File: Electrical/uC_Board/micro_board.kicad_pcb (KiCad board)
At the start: 2 copper layers, 45 x 18 mm, 26 parts, among them J1 card_edge_6p, Q1 BC850, SW1 SW_Push, U1 ATmega328PB-AU, U2 ArdStripNano, U3 CSTNE16M0V530000R0, U4 AD8620, U5 LM1117MPX-5.0

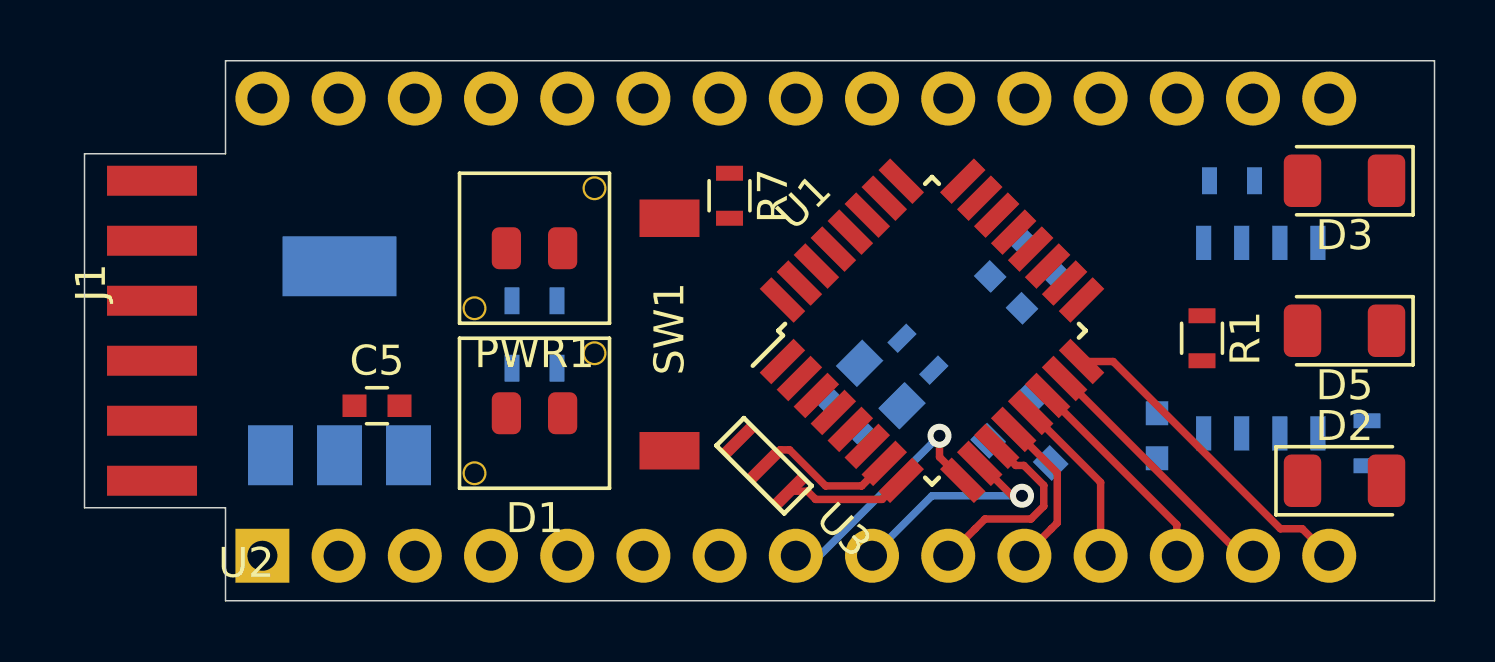
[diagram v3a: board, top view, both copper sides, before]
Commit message: adding traces, removed auto selector, changed diode footprints
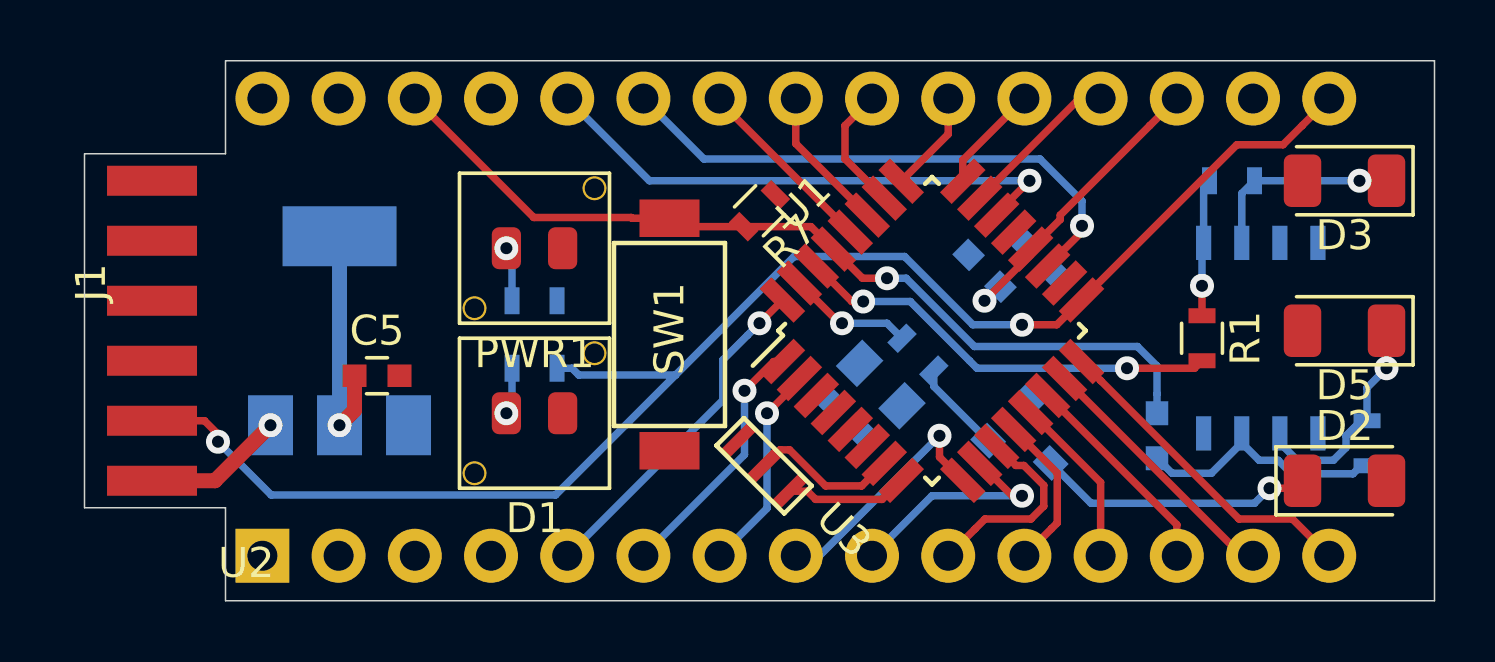
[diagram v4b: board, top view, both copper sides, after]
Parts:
- moved R7 1.12 mm to (122.5, 96.0), turned to 225 degrees
- moved C4 1.02 mm to (130.0, 98.0), turned to 135 degrees
- moved C5 1.00 mm to (109.8, 101.5)
- moved U5 1.00 mm to (108.5, 100.0)
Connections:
- C4 pad 1: Net-(C4-Pad1) -> /AREF
- U1 pad 20: Net-(C4-Pad1) -> /AREF
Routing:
- net /D13: track 0.00 -> 51.8 mm, vias 0 -> 2
- net /RESET: track 0.00 -> 30.0 mm, vias 0 -> 1
- net /A6: track 0.00 -> 18.7 mm, vias 0 -> 1
- net /A7: track 0.00 -> 18.1 mm, vias 0 -> 1
- net /D0: track 0.00 -> 14.4 mm, vias 0 -> 2
- net /D2: track 0.00 -> 11.5 mm, vias 0 -> 1
- net /AREF: track 0.00 -> 10.1 mm, vias 0 -> 1
- net Net-(D2-Pad1): track 0.00 -> 9.26 mm, vias 0 -> 1
- net /D3: track 0.00 -> 8.56 mm, vias 0 -> 1
- net Net-(C6-Pad1): track 0.00 -> 8.48 mm
- net +5V: track 0.00 -> 8.16 mm, vias 0 -> 1
- net Net-(D5-Pad1): track 0.00 -> 7.51 mm, vias 0 -> 1
- net /D4: track 0.00 -> 7.01 mm, vias 0 -> 1
- net Net-(D3-Pad1): track 0.00 -> 6.65 mm, vias 0 -> 1
- net /A5: track 0.00 -> 6.26 mm
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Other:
- net class power added: clearance 0.2, trace_width 0.5, via_dia 0.8, via_drill 0.4

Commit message: i have no idea where these last traces are supposed to go
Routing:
- net /RESET: track 30.0 -> 43.7 mm
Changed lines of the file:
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@@
     (thickness 1.6)
     (drawings 9)
-    (tracks 198)
+    (tracks 202)
     (zones 0)
     (modules 26)
@@
     (38 B.Mask user)
     (39 F.Mask user)
-    (40 Dwgs.User user)
+    (40 Dwgs.User user hide)
     (41 Cmts.User user)
     (42 Eco1.User user)
@@
   (segment (start 114.97499 96.22499) (end 118.22499 96.22499) (width 0.25) (layer F.Cu) (net 5))
   (segment (start 111.01 92.26) (end 114.97499 96.22499) (width 0.25) (layer F.Cu) (net 5))
+  (segment (start 113.58316 96.22499) (end 114.97499 96.22499) (width 0.25) (layer F.Cu) (net 5))
+  (segment (start 111.909999 97.898151) (end 113.58316 96.22499) (width 0.25) (layer F.Cu) (net 5))
+  (segment (start 111.909999 106.600001) (end 111.909999 97.898151) (width 0.25) (layer F.Cu) (net 5))
+  (segment (start 111.01 107.5) (end 111.909999 106.600001) (width 0.25) (layer F.Cu) (net 5))
   (segment (start 138.578427 107.5) (end 138.95 107.5) (width 0.25) (layer F.Cu) (net 6))
   (segment (start 132.669417 101.59099) (end 138.578427 107.5) (width 0.25) (layer F.Cu) (net 6))

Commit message: forgot a file
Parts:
- moved C5 1.25 mm to (109.8, 100.2)
- moved U5 1.25 mm to (108.5, 98.8)
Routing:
- net /D1: track 4.18 -> 30.0 mm
- net VCC: track 4.72 -> 0.00 mm, vias 1 -> 0
- net /RESET: track 43.7 -> 44.1 mm, vias 1 -> 2
- net /D13: track 51.8 -> 51.7 mm, vias 2 -> 4
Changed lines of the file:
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@@
     (thickness 1.6)
     (drawings 9)
-    (tracks 202)
+    (tracks 219)
     (zones 0)
     (modules 26)
@@
   )
   (module hodgkin:LM1117 (layer B.Cu)
-    (at 108.5 100 90)
+    (at 108.5 98.75 90)
     (descr "module CMS SOT223 4 pins")
     (tags "CMS SOT")
@@
   )
   (module Capacitors_SMD:C_0603 (layer F.Cu)
-    (at 109.75 101.5)
+    (at 109.75 100.25)
     (descr "Capacitor SMD 0603, reflow soldering, AVX (see smccp.pdf)")
     (tags "capacitor 0603")
@@
   (gr_line (start 145 91) (end 145 109) (layer Edge.Cuts) (width 0.05))
   (gr_line (start 104.7 109) (end 145 109) (layer Edge.Cuts) (width 0.05))
-  (via (at 106.2 103.15) (size 0.8) (drill 0.4) (layers F.Cu B.Cu) (net 2))
-  (segment (start 104.35 105) (end 102.25 105) (width 0.5) (layer F.Cu) (net 2))
-  (segment (start 106.2 103.15) (end 104.35 105) (width 0.5) (layer F.Cu) (net 2))
   (via (at 114.0625 102.75) (size 0.8) (drill 0.4) (layers F.Cu B.Cu) (net 3))
   (segment (start 114.25 101.25) (end 114.25 102.5625) (width 0.25) (layer B.Cu) (net 3))
@@
   (segment (start 111.01 92.26) (end 114.97499 96.22499) (width 0.25) (layer F.Cu) (net 5))
   (segment (start 113.58316 96.22499) (end 114.97499 96.22499) (width 0.25) (layer F.Cu) (net 5))
-  (segment (start 111.909999 97.898151) (end 113.58316 96.22499) (width 0.25) (layer F.Cu) (net 5))
-  (segment (start 111.909999 106.600001) (end 111.909999 97.898151) (width 0.25) (layer F.Cu) (net 5))
-  (segment (start 111.01 107.5) (end 111.909999 106.600001) (width 0.25) (layer F.Cu) (net 5))
+  (via (at 113 96.25) (size 0.8) (drill 0.4) (layers F.Cu B.Cu) (net 5))
+  (segment (start 111.909999 97.340001) (end 113 96.25) (width 0.25) (layer B.Cu) (net 5))
+  (segment (start 111.01 107.5) (end 111.909999 106.600001) (width 0.25) (layer B.Cu) (net 5))
+  (segment (start 111.909999 106.600001) (end 111.909999 97.340001) (width 0.25) (layer B.Cu) (net 5))
+  (segment (start 113.58316 96.232525) (end 113.58316 96.22499) (width 0.25) (layer F.Cu) (net 5))
+  (segment (start 113.565685 96.25) (end 113.58316 96.232525) (width 0.25) (layer F.Cu) (net 5))
+  (segment (start 113 96.25) (end 113.565685 96.25) (width 0.25) (layer F.Cu) (net 5))
   (segment (start 138.578427 107.5) (end 138.95 107.5) (width 0.25) (layer F.Cu) (net 6))
   (segment (start 132.669417 101.59099) (end 138.578427 107.5) (width 0.25) (layer F.Cu) (net 6))
@@
   (segment (start 132.409799 99.799999) (end 133.235103 98.974695) (width 0.25) (layer F.Cu) (net 7))
   (segment (start 131.25 99.799999) (end 132.409799 99.799999) (width 0.25) (layer F.Cu) (net 7))
-  (via (at 104.448959 103.698959) (size 0.8) (drill 0.4) (layers F.Cu B.Cu) (net 7))
-  (segment (start 104.448959 103.448959) (end 104.448959 103.698959) (width 0.25) (layer F.Cu) (net 7))
-  (segment (start 102.25 103) (end 104 103) (width 0.25) (layer F.Cu) (net 7))
-  (segment (start 104 103) (end 104.448959 103.448959) (width 0.25) (layer F.Cu) (net 7))
-  (segment (start 115.701997 105.475001) (end 119.701997 101.475001) (width 0.25) (layer B.Cu) (net 7))
-  (segment (start 106.225001 105.475001) (end 115.701997 105.475001) (width 0.25) (layer B.Cu) (net 7))
-  (segment (start 104.448959 103.698959) (end 106.225001 105.475001) (width 0.25) (layer B.Cu) (net 7))
-  (segment (start 108.5 96.85) (end 108.5 103.15) (width 0.5) (layer B.Cu) (net 8))
-  (via (at 108.5 103.15) (size 0.8) (drill 0.4) (layers F.Cu B.Cu) (net 8))
-  (segment (start 109 101.5) (end 109 102.65) (width 0.5) (layer F.Cu) (net 8))
-  (segment (start 109 102.65) (end 108.5 103.15) (width 0.5) (layer F.Cu) (net 8))
+  (via (at 118.75 102.25) (size 0.8) (drill 0.4) (layers F.Cu B.Cu) (net 7))
+  (segment (start 119.701997 101.475001) (end 119.524999 101.475001) (width 0.25) (layer B.Cu) (net 7))
+  (segment (start 119.524999 101.475001) (end 118.75 102.25) (width 0.25) (layer B.Cu) (net 7))
+  (segment (start 118.75 102.25) (end 115.524999 105.475001) (width 0.25) (layer F.Cu) (net 7))
+  (segment (start 112.651999 105.475001) (end 115.524999 105.475001) (width 0.25) (layer F.Cu) (net 7))
+  (via (at 108 105.5) (size 0.8) (drill 0.4) (layers F.Cu B.Cu) (net 7))
+  (segment (start 112.651999 105.475001) (end 108.024999 105.475001) (width 0.25) (layer F.Cu) (net 7))
+  (segment (start 108.024999 105.475001) (end 108 105.5) (width 0.25) (layer F.Cu) (net 7))
+  (via (at 106 105) (size 0.8) (drill 0.4) (layers F.Cu B.Cu) (net 7))
+  (segment (start 108 105.5) (end 106.5 105.5) (width 0.25) (layer B.Cu) (net 7))
+  (segment (start 106.5 105.5) (end 106 105) (width 0.25) (layer B.Cu) (net 7))
+  (segment (start 104 103) (end 102.25 103) (width 0.25) (layer F.Cu) (net 7))
+  (segment (start 106 105) (end 104 103) (width 0.25) (layer F.Cu) (net 7))
+  (segment (start 108.5 95.6) (end 108.5 101.9) (width 0.5) (layer B.Cu) (net 8))
+  (via (at 108.5 101.9) (size 0.8) (drill 0.4) (layers F.Cu B.Cu) (net 8))
+  (segment (start 109 100.25) (end 109 101.4) (width 0.5) (layer F.Cu) (net 8))
+  (segment (start 109 101.4) (end 108.5 101.9) (width 0.5) (layer F.Cu) (net 8))
   (segment (start 133.871498 101.6617) (end 133.235103 101.025305) (width 0.25) (layer F.Cu) (net 9))
   (segment (start 138.484797 106.274999) (end 133.871498 101.6617) (width 0.25) (layer F.Cu) (net 9))
@@
   (segment (start 125.171573 99.75) (end 123.830583 98.40901) (width 0.25) (layer F.Cu) (net 14))
   (segment (start 125.25 99.75) (end 125.171573 99.75) (width 0.25) (layer F.Cu) (net 14))
+  (segment (start 108.339999 99.549999) (end 107.25 100.639998) (width 0.25) (layer F.Cu) (net 14))
+  (segment (start 123.171573 97.75) (end 116.94185 97.75) (width 0.25) (layer F.Cu) (net 14))
+  (segment (start 123.830583 98.40901) (end 123.171573 97.75) (width 0.25) (layer F.Cu) (net 14))
+  (segment (start 116.94185 97.75) (end 114.716849 99.975001) (width 0.25) (layer F.Cu) (net 14))
+  (segment (start 114.716849 99.975001) (end 111.585003 99.975001) (width 0.25) (layer F.Cu) (net 14))
+  (segment (start 111.585003 99.975001) (end 111.160001 99.549999) (width 0.25) (layer F.Cu) (net 14))
+  (segment (start 111.160001 99.549999) (end 108.339999 99.549999) (width 0.25) (layer F.Cu) (net 14))
+  (segment (start 105.93 106.35) (end 105.93 107.5) (width 0.25) (layer F.Cu) (net 14))
+  (segment (start 107.25 105.03) (end 105.93 106.35) (width 0.25) (layer F.Cu) (net 14))
+  (segment (start 107.25 100.639998) (end 107.25 105.03) (width 0.25) (layer F.Cu) (net 14))
   (via (at 122.5 99.75) (size 0.8) (drill 0.4) (layers F.Cu B.Cu) (net 15))
   (segment (start 123.264897 98.974695) (end 123.264897 98.985103) (width 0.25) (layer F.Cu) (net 15))

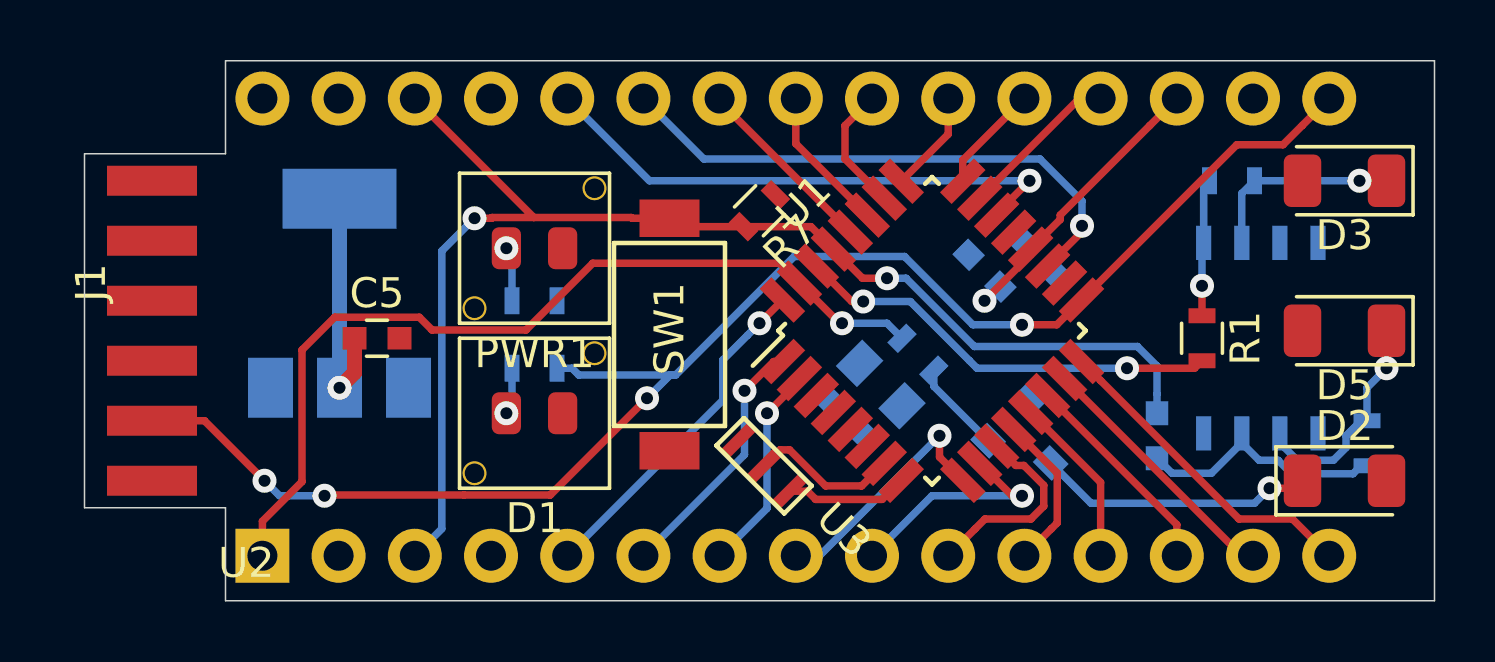
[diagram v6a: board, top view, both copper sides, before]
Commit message: changed atmega, started re-laying traces
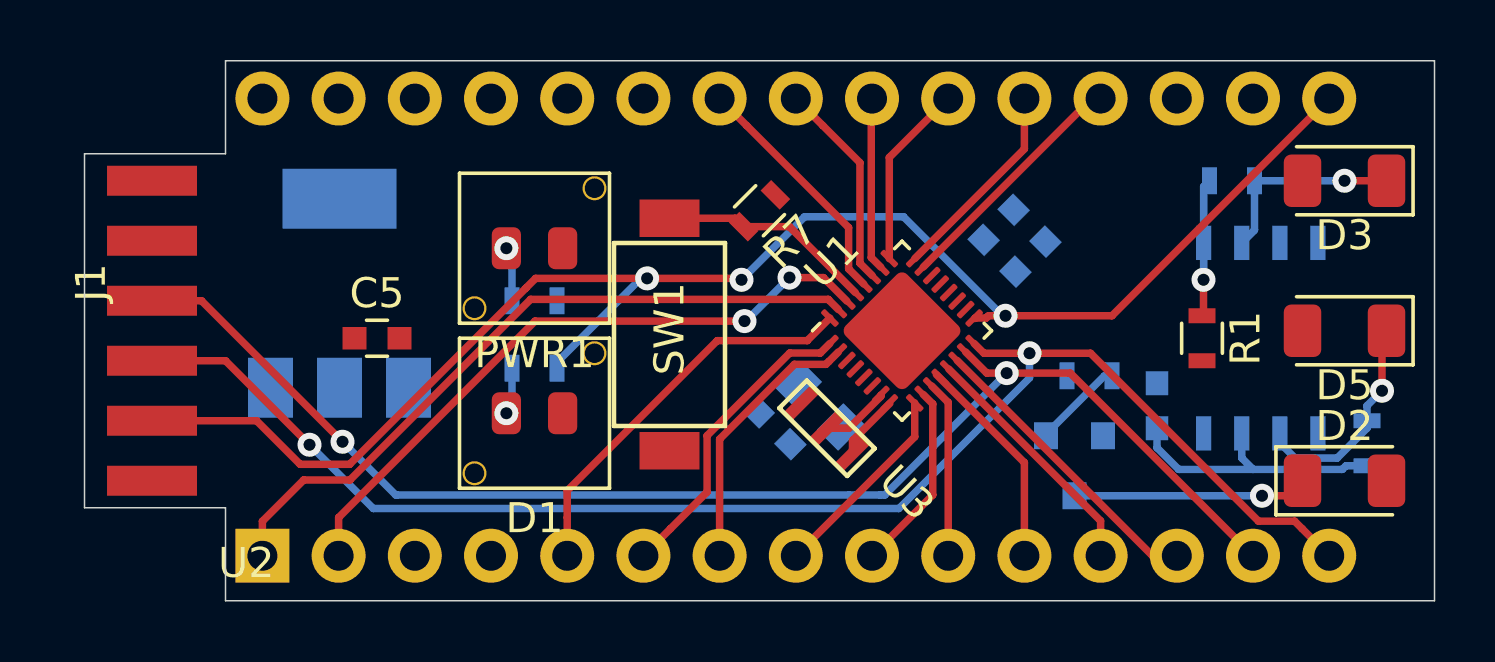
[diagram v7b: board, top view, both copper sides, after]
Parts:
- U1: footprint hodgkin:TQFP-32_7x7mm_P0.8mm -> hodgkin:QFN-32-1EP_4x4mm_P0.4mm_EP2.9x2.9mm
- moved R2 5.76 mm to (133.5, 101.5), turned to 180 degrees
- moved U3 2.44 mm to (126.3, 103.9)
- moved C1 2.28 mm to (123.0, 103.2), turned to 135 degrees
- moved C2 2.16 mm to (124.5, 102.5)
- moved Q1 1.70 mm to (133.0, 104.5), turned to 270 degrees
- moved C6 1.00 mm to (135.8, 102.5)
- moved U1 1.00 mm to (127.2, 100.0)
- moved C3 0.99 mm to (131.5, 96.5)
- moved C4 0.71 mm to (130.5, 97.5)
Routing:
- net /D12: track 10.9 -> 48.7 mm, vias 0 -> 2
- net /D11: track 8.73 -> 45.2 mm, vias 0 -> 2
- net /RESET: track 44.1 -> 7.62 mm, vias 2 -> 0
- net /A6: track 18.7 -> 0.00 mm, vias 1 -> 0
- net /A7: track 18.1 -> 0.00 mm, vias 1 -> 0
- net /AREF: track 10.1 -> 0.00 mm, vias 1 -> 0
- net +5V: track 8.16 -> 0.00 mm, vias 1 -> 0
- net /D0: track 14.4 -> 21.9 mm
- net /D1: track 30.0 -> 23.6 mm, vias 1 -> 0
- net /A1: track 3.61 -> 6.85 mm
- net /D10: track 7.13 -> 10.0 mm
- net /A0: track 5.40 -> 8.24 mm
- net Net-(U1-Pad7): track 5.04 -> 2.29 mm
- net /A2: track 3.40 -> 6.15 mm
- net /D9: track 5.74 -> 8.32 mm
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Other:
- net class Default: clearance 0.2 -> 0.127
- rule trace_clearance: 0.2 -> 0.127

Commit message: finished first try of traces, problems with GND plane
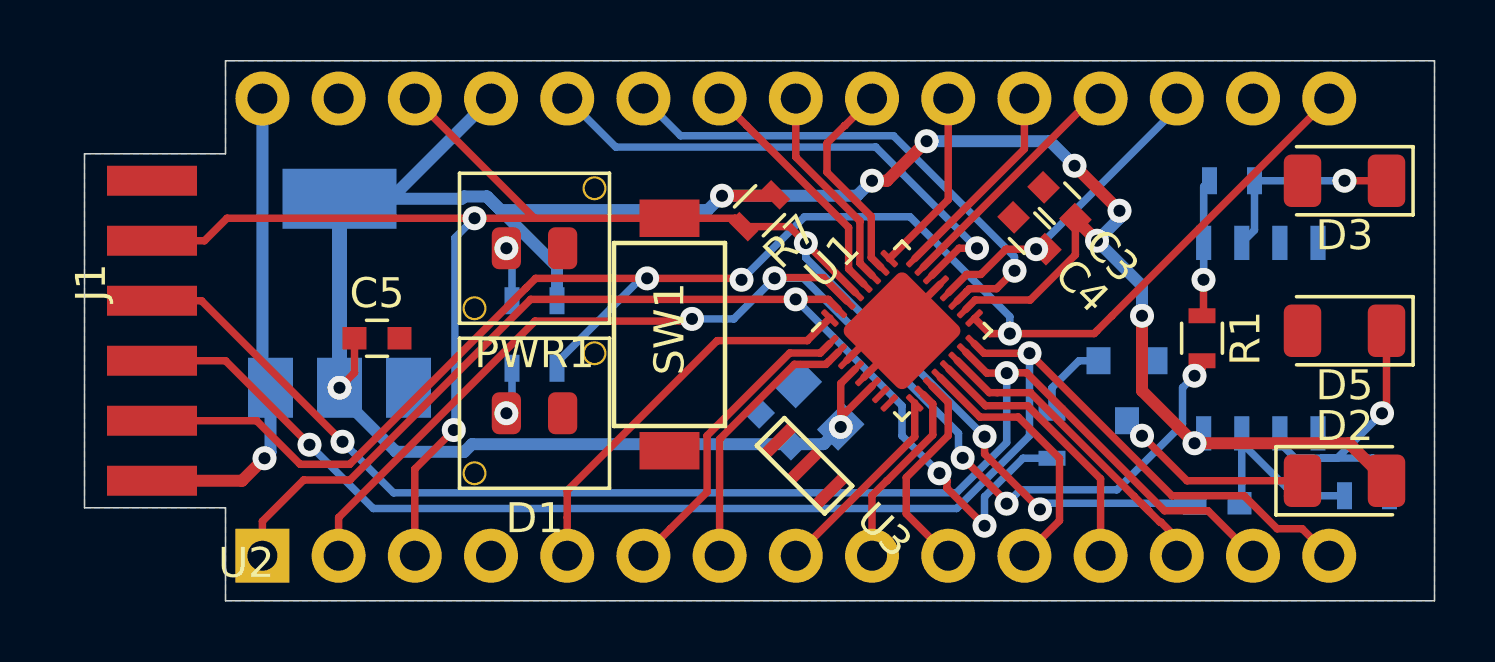
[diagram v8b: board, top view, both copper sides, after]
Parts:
- C3, C4: moved to F.Cu
- moved C6 3.82 mm to (137.8, 105.8), turned to 180 degrees
- moved Q1 3.05 mm to (134.8, 102.0)
- moved R2 2.36 mm to (132.2, 103.5), turned to 270 degrees
- moved R8 1.75 mm to (142.8, 105.5), turned to 0 degrees
- moved U3 1.46 mm to (125.6, 105.2)
- moved C3 1.25 mm to (132.5, 95.8)
- moved C4 1.25 mm to (131.5, 96.8)
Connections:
- U1 pad 33: (no net) -> GND
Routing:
- net +5V: track 0.00 -> 94.4 mm, vias 0 -> 10
- net /RESET: track 7.62 -> 60.2 mm, vias 0 -> 5
- net /D0: track 21.9 -> 42.5 mm, vias 2 -> 5
- net /A7: track 0.00 -> 17.6 mm, vias 0 -> 1
- net /A6: track 0.00 -> 17.3 mm, vias 0 -> 1
- net VCC: track 0.00 -> 16.2 mm, vias 0 -> 1
- net /D1: track 23.6 -> 37.5 mm, vias 0 -> 3
- net /AREF: track 0.00 -> 10.8 mm, vias 0 -> 1
- net GND: track 0.00 -> 6.41 mm
- net Net-(D5-Pad1): track 7.36 -> 10.5 mm
- net Net-(C6-Pad1): track 9.36 -> 6.83 mm
- net Net-(U1-Pad7): track 2.29 -> 0.00 mm
- net Net-(U1-Pad8): track 2.19 -> 0.00 mm
- net /D8: track 7.25 -> 8.83 mm
- net /D11: track 45.2 -> 46.6 mm
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- added copper zone on B.Cu, net GND
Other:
- net class power removed
